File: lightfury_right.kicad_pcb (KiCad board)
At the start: 6 copper layers, 156 x 116.5 mm, 89 parts, among them U1 TLV61070ADBV, U2 SN74LV1T126DBVR

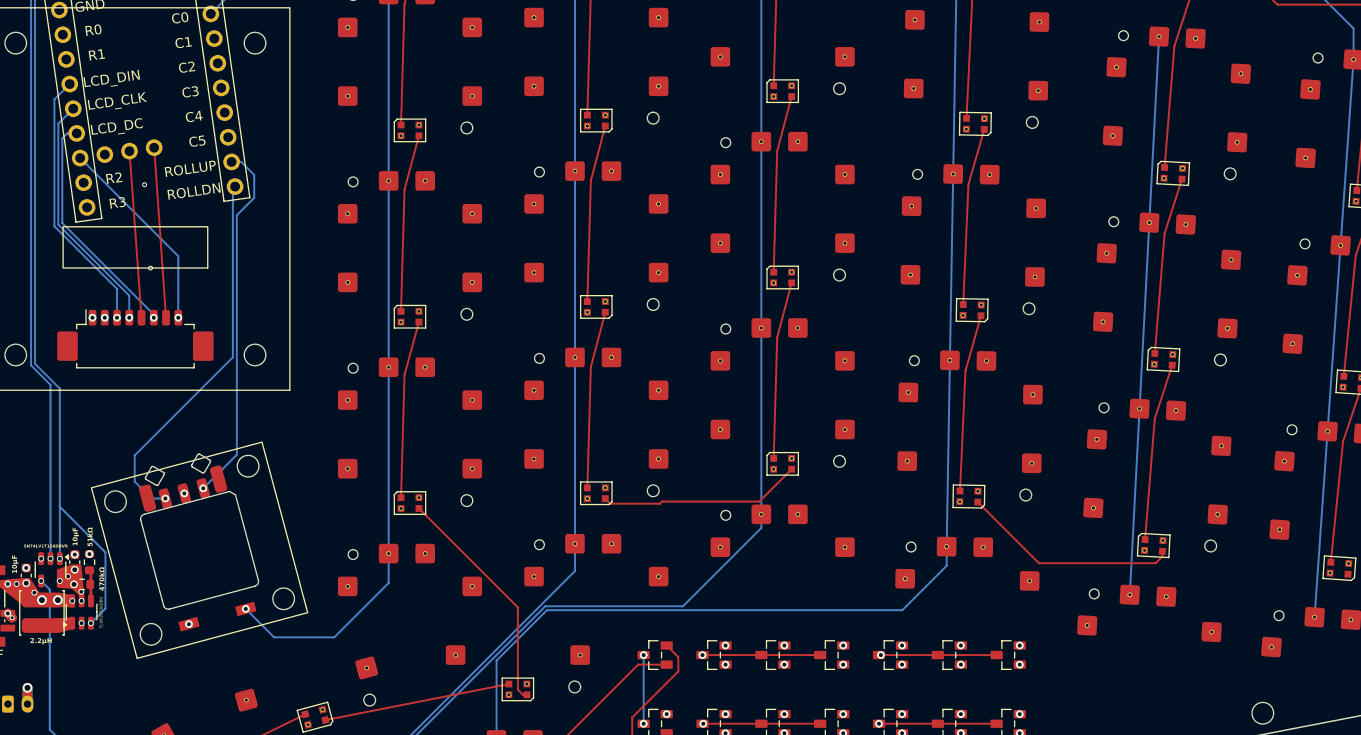
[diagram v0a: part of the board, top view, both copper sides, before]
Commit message: Added capacitors for 5v load smoothing.
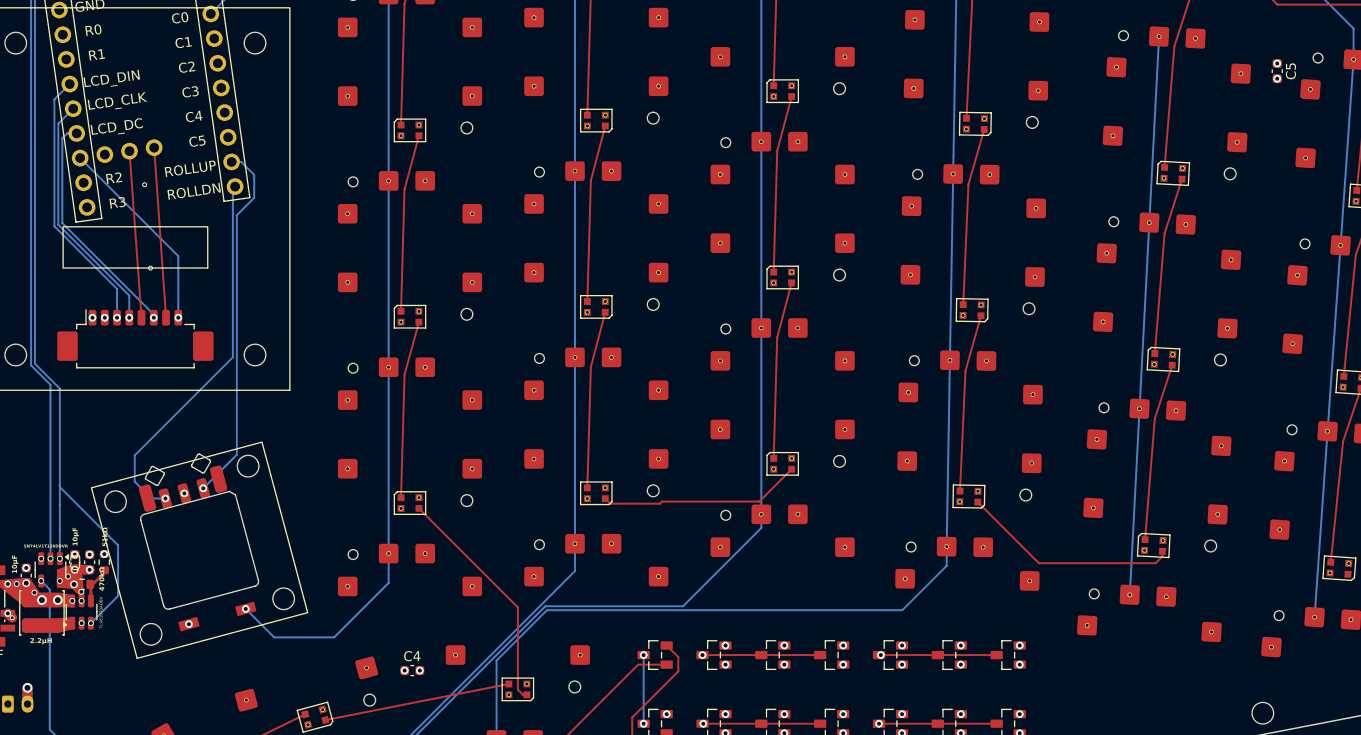
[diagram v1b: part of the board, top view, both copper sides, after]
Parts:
- added C3: 100nF, Capacitor_SMD:C_0603_1608Metric, F.Cu at (231.3, 157.4)
- added C4: 10μF, Capacitor_SMD:C_0603_1608Metric, F.Cu at (264.2, 168.5)
- added C5: 10μF, Capacitor_SMD:C_0603_1608Metric, F.Cu at (352.4, 107.3)
- moved R2 1.51 mm to (232.8, 157.4)
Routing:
- net 5V: track 6.04 -> 15.1 mm, vias 6 -> 9
- net 5V_EN: track 77.3 -> 80.4 mm
- net BOOST_FB: track 3.18 -> 3.69 mm
- net GND: vias 11 -> 14

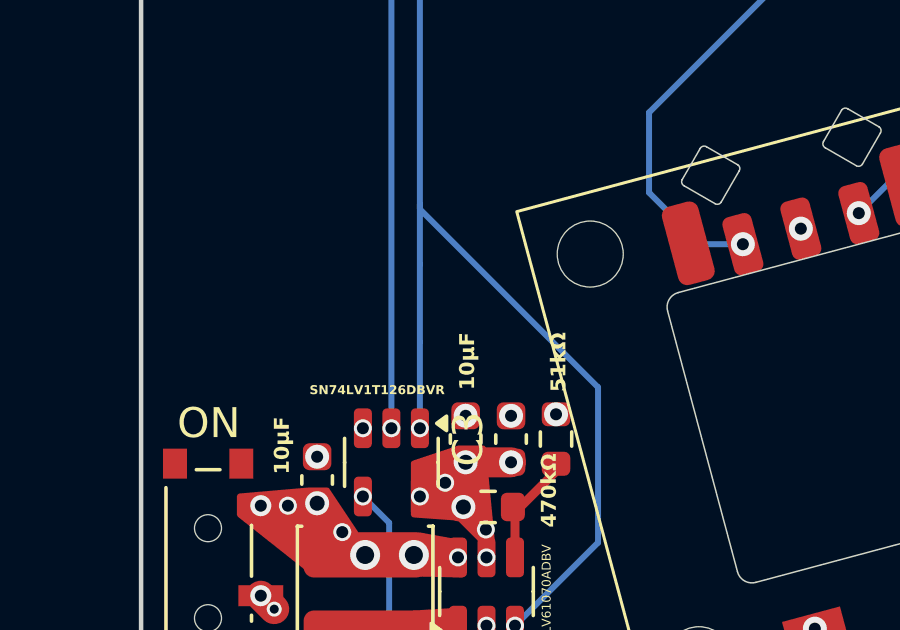
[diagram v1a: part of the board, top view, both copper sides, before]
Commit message: Add LCSC field and populate for BOM.
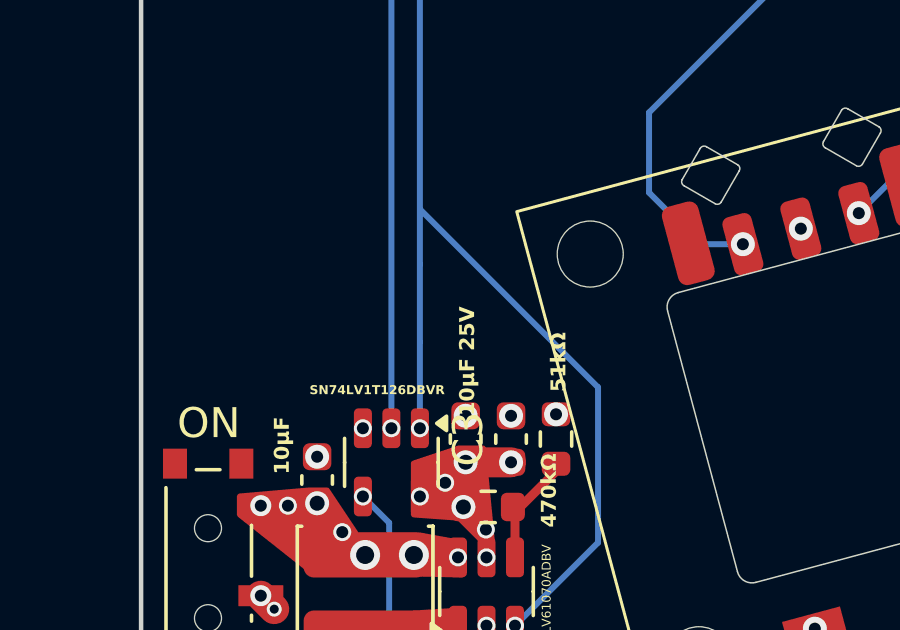
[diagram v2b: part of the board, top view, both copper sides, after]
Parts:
- C2, C4, C5: value 10μF -> 10μF 25V
